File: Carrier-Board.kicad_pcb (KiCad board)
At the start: 2 copper layers, 1 part, among them X1 PC104_PLUS

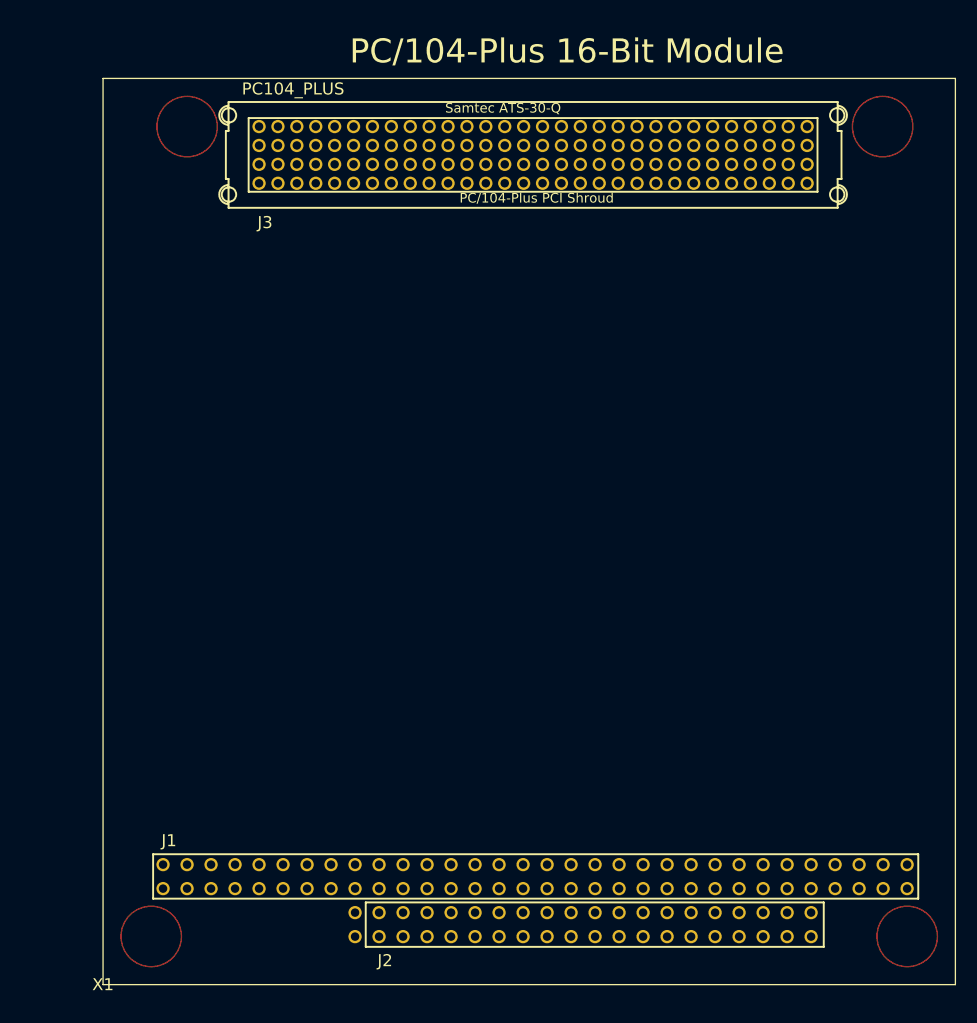
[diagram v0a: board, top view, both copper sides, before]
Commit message: Misc footprint stuff and ethernet
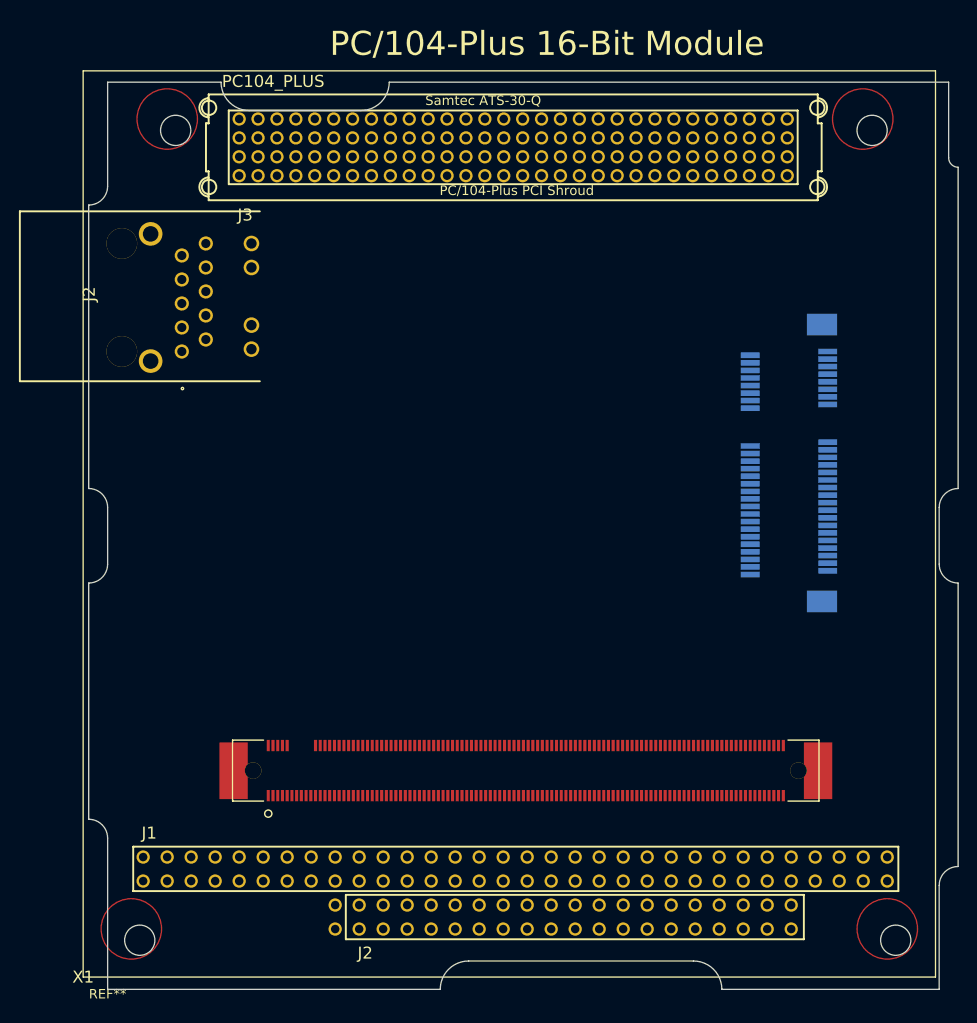
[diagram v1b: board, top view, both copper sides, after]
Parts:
- added J1: CONN_3-6318491-6, Carrier-Board:ComExpressMini10, F.Cu at (66.5, 101.7)
- added J2: SI-51009-F, Carrier-Board:SI-51009-F, F.Cu at (47.7, 54.2)
- added REF**: pc104, Carrier-Board:pc104, F.Cu at (57.0, 127.5)
- added U1: MSATA-Socket, Carrier-Board:msata-socket, B.Cu at (129.1, 59.3)
- moved X1 2.25 mm to (54.4, 126.2)
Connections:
- X1 pad A1: (no net) -> Net-(X1-PadA1)
- X1 pad A10: (no net) -> Net-(X1-PadA10)
- X1 pad A11: (no net) -> Net-(X1-PadA11)
- X1 pad A12: (no net) -> Net-(X1-PadA12)
- X1 pad A13: (no net) -> Net-(X1-PadA13)
- X1 pad A14: (no net) -> Net-(X1-PadA14)
- X1 pad A15: (no net) -> Net-(X1-PadA15)
- X1 pad A16: (no net) -> Net-(X1-PadA16)
- X1 pad A17: (no net) -> Net-(X1-PadA17)
- X1 pad A18: (no net) -> Net-(X1-PadA18)
- X1 pad A19: (no net) -> Net-(X1-PadA19)
- X1 pad A2: (no net) -> Net-(X1-PadA2)
- X1 pad A20: (no net) -> Net-(X1-PadA20)
- X1 pad A21: (no net) -> Net-(X1-PadA21)
- X1 pad A22: (no net) -> Net-(X1-PadA22)
- X1 pad A23: (no net) -> Net-(X1-PadA23)
- X1 pad A24: (no net) -> Net-(X1-PadA24)
- X1 pad A25: (no net) -> Net-(X1-PadA25)
- X1 pad A26: (no net) -> Net-(X1-PadA26)
- X1 pad A27: (no net) -> Net-(X1-PadA27)
- X1 pad A28: (no net) -> Net-(X1-PadA28)
- X1 pad A29: (no net) -> Net-(X1-PadA29)
- X1 pad A3: (no net) -> Net-(X1-PadA3)
- X1 pad A30: (no net) -> Net-(X1-PadA30)
- X1 pad A31: (no net) -> Net-(X1-PadA31)
- X1 pad A32: (no net) -> Net-(X1-PadA32)
- X1 pad A4: (no net) -> Net-(X1-PadA4)
- X1 pad A5: (no net) -> Net-(X1-PadA5)
- X1 pad A6: (no net) -> Net-(X1-PadA6)
- X1 pad A7: (no net) -> Net-(X1-PadA7)
- X1 pad A8: (no net) -> Net-(X1-PadA8)
- X1 pad A9: (no net) -> Net-(X1-PadA9)
- X1 pad B1: (no net) -> Net-(X1-PadB1)
- X1 pad B10: (no net) -> Net-(X1-PadB10)
- X1 pad B11: (no net) -> Net-(X1-PadB11)
- X1 pad B12: (no net) -> Net-(X1-PadB12)
- X1 pad B13: (no net) -> Net-(X1-PadB13)
- X1 pad B14: (no net) -> Net-(X1-PadB14)
- X1 pad B15: (no net) -> Net-(X1-PadB15)
- X1 pad B16: (no net) -> Net-(X1-PadB16)
- X1 pad B17: (no net) -> Net-(X1-PadB17)
- X1 pad B18: (no net) -> Net-(X1-PadB18)
- X1 pad B19: (no net) -> Net-(X1-PadB19)
- X1 pad B2: (no net) -> Net-(X1-PadB2)
- X1 pad B20: (no net) -> Net-(X1-PadB20)
- X1 pad B21: (no net) -> Net-(X1-PadB21)
- X1 pad B22: (no net) -> Net-(X1-PadB22)
- X1 pad B23: (no net) -> Net-(X1-PadB23)
- X1 pad B24: (no net) -> Net-(X1-PadB24)
- X1 pad B25: (no net) -> Net-(X1-PadB25)
- X1 pad B26: (no net) -> Net-(X1-PadB26)
- X1 pad B27: (no net) -> Net-(X1-PadB27)
- X1 pad B28: (no net) -> Net-(X1-PadB28)
- X1 pad B29: (no net) -> Net-(X1-PadB29)
- X1 pad B3: (no net) -> Net-(X1-PadB3)
- X1 pad B30: (no net) -> Net-(X1-PadB30)
- X1 pad B31: (no net) -> Net-(X1-PadB31)
- X1 pad B32: (no net) -> Net-(X1-PadB32)
- X1 pad B4: (no net) -> Net-(X1-PadB4)
- X1 pad B5: (no net) -> Net-(X1-PadB5)
- X1 pad B6: (no net) -> Net-(X1-PadB6)
- X1 pad B7: (no net) -> Net-(X1-PadB7)
- X1 pad B8: (no net) -> Net-(X1-PadB8)
- X1 pad B9: (no net) -> Net-(X1-PadB9)
- X1 pad C0: (no net) -> Net-(X1-PadC0)
- X1 pad C1: (no net) -> Net-(X1-PadC1)
- X1 pad C10: (no net) -> Net-(X1-PadC10)
- X1 pad C11: (no net) -> Net-(X1-PadC11)
- X1 pad C12: (no net) -> Net-(X1-PadC12)
- X1 pad C13: (no net) -> Net-(X1-PadC13)
- X1 pad C14: (no net) -> Net-(X1-PadC14)
- X1 pad C15: (no net) -> Net-(X1-PadC15)
- X1 pad C16: (no net) -> Net-(X1-PadC16)
- X1 pad C17: (no net) -> Net-(X1-PadC17)
- X1 pad C18: (no net) -> Net-(X1-PadC18)
- X1 pad C19: (no net) -> Net-(X1-PadC19)
- X1 pad C2: (no net) -> Net-(X1-PadC2)
- X1 pad C3: (no net) -> Net-(X1-PadC3)
- X1 pad C4: (no net) -> Net-(X1-PadC4)
- X1 pad C5: (no net) -> Net-(X1-PadC5)
- X1 pad C6: (no net) -> Net-(X1-PadC6)
- X1 pad C7: (no net) -> Net-(X1-PadC7)
- X1 pad C8: (no net) -> Net-(X1-PadC8)
- X1 pad C9: (no net) -> Net-(X1-PadC9)
- X1 pad D0: (no net) -> Net-(X1-PadD0)
- X1 pad D1: (no net) -> Net-(X1-PadD1)
- X1 pad D10: (no net) -> Net-(X1-PadD10)
- X1 pad D11: (no net) -> Net-(X1-PadD11)
- X1 pad D12: (no net) -> Net-(X1-PadD12)
- X1 pad D13: (no net) -> Net-(X1-PadD13)
- X1 pad D14: (no net) -> Net-(X1-PadD14)
- X1 pad D15: (no net) -> Net-(X1-PadD15)
- X1 pad D16: (no net) -> Net-(X1-PadD16)
- X1 pad D17: (no net) -> Net-(X1-PadD17)
- X1 pad D18: (no net) -> Net-(X1-PadD18)
- X1 pad D19: (no net) -> Net-(X1-PadD19)
- X1 pad D2: (no net) -> Net-(X1-PadD2)
- X1 pad D3: (no net) -> Net-(X1-PadD3)
- X1 pad D4: (no net) -> Net-(X1-PadD4)
- X1 pad D5: (no net) -> Net-(X1-PadD5)
- X1 pad D6: (no net) -> Net-(X1-PadD6)
- X1 pad D7: (no net) -> Net-(X1-PadD7)
- X1 pad D8: (no net) -> Net-(X1-PadD8)
- X1 pad D9: (no net) -> Net-(X1-PadD9)
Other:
- board outline added: 92 x 96 mm

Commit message: Remove junk from pc104
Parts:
- removed X1: PC104_PLUS, Carrier-Board:con-pc104-PC104-PLUS
- added J1: PC104_PLUS, Carrier-Board:pc104_silk, F.Cu at (54.4, 126.1)
- J2: renamed from J1; value CONN_3-6318491-6 -> PC104_PLUS
- renumbered J2 to J3
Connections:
- J2 pad 1: Net-(J1-Pad1) -> (no net)
- J2 pad 10: Net-(J1-Pad10) -> (no net)
- J2 pad 100: Net-(J1-Pad100) -> (no net)
- J2 pad 101: Net-(J1-Pad101) -> (no net)
- J2 pad 102: Net-(J1-Pad102) -> (no net)
- J2 pad 103: Net-(J1-Pad103) -> (no net)
- J2 pad 104: Net-(J1-Pad104) -> (no net)
- J2 pad 105: Net-(J1-Pad105) -> (no net)
- J2 pad 106: Net-(J1-Pad106) -> (no net)
- J2 pad 107: Net-(J1-Pad107) -> (no net)
- J2 pad 108: Net-(J1-Pad108) -> (no net)
- J2 pad 109: Net-(J1-Pad109) -> (no net)
- J2 pad 11: Net-(J1-Pad11) -> (no net)
- J2 pad 110: Net-(J1-Pad110) -> (no net)
- J2 pad 111: Net-(J1-Pad111) -> (no net)
- J2 pad 112: Net-(J1-Pad112) -> (no net)
- J2 pad 113: Net-(J1-Pad113) -> (no net)
- J2 pad 114: Net-(J1-Pad114) -> (no net)
- J2 pad 115: Net-(J1-Pad115) -> (no net)
- J2 pad 12: Net-(J1-Pad12) -> (no net)
- J2 pad 121: Net-(J1-Pad121) -> (no net)
- J2 pad 122: Net-(J1-Pad122) -> (no net)
- J2 pad 123: Net-(J1-Pad123) -> (no net)
- J2 pad 124: Net-(J1-Pad124) -> (no net)
- J2 pad 125: Net-(J1-Pad125) -> (no net)
- J2 pad 126: Net-(J1-Pad126) -> (no net)
- J2 pad 127: Net-(J1-Pad127) -> (no net)
- J2 pad 128: Net-(J1-Pad128) -> (no net)
- J2 pad 129: Net-(J1-Pad129) -> (no net)
- J2 pad 13: Net-(J1-Pad13) -> (no net)
- J2 pad 130: Net-(J1-Pad130) -> (no net)
- J2 pad 131: Net-(J1-Pad131) -> (no net)
- J2 pad 132: Net-(J1-Pad132) -> (no net)
- J2 pad 133: Net-(J1-Pad133) -> (no net)
- J2 pad 134: Net-(J1-Pad134) -> (no net)
- J2 pad 135: Net-(J1-Pad135) -> (no net)
- J2 pad 136: Net-(J1-Pad136) -> (no net)
- J2 pad 137: Net-(J1-Pad137) -> (no net)
- J2 pad 138: Net-(J1-Pad138) -> (no net)
- J2 pad 139: Net-(J1-Pad139) -> (no net)
- J2 pad 14: Net-(J1-Pad14) -> (no net)
- J2 pad 140: Net-(J1-Pad140) -> (no net)
- J2 pad 141: Net-(J1-Pad141) -> (no net)
- J2 pad 142: Net-(J1-Pad142) -> (no net)
- J2 pad 143: Net-(J1-Pad143) -> (no net)
- J2 pad 144: Net-(J1-Pad144) -> (no net)
- J2 pad 145: Net-(J1-Pad145) -> (no net)
- J2 pad 146: Net-(J1-Pad146) -> (no net)
- J2 pad 147: Net-(J1-Pad147) -> (no net)
- J2 pad 148: Net-(J1-Pad148) -> (no net)
- J2 pad 149: Net-(J1-Pad149) -> (no net)
- J2 pad 15: Net-(J1-Pad15) -> (no net)
- J2 pad 150: Net-(J1-Pad150) -> (no net)
- J2 pad 151: Net-(J1-Pad151) -> (no net)
- J2 pad 152: Net-(J1-Pad152) -> (no net)
- J2 pad 153: Net-(J1-Pad153) -> (no net)
- J2 pad 154: Net-(J1-Pad154) -> (no net)
- J2 pad 155: Net-(J1-Pad155) -> (no net)
- J2 pad 156: Net-(J1-Pad156) -> (no net)
- J2 pad 157: Net-(J1-Pad157) -> (no net)
- J2 pad 158: Net-(J1-Pad158) -> (no net)
- J2 pad 159: Net-(J1-Pad159) -> (no net)
- J2 pad 16: Net-(J1-Pad16) -> (no net)
- J2 pad 160: Net-(J1-Pad160) -> (no net)
- J2 pad 161: Net-(J1-Pad161) -> (no net)
- J2 pad 162: Net-(J1-Pad162) -> (no net)
- J2 pad 163: Net-(J1-Pad163) -> (no net)
- J2 pad 164: Net-(J1-Pad164) -> (no net)
- J2 pad 165: Net-(J1-Pad165) -> (no net)
- J2 pad 166: Net-(J1-Pad166) -> (no net)
- J2 pad 167: Net-(J1-Pad167) -> (no net)
- J2 pad 168: Net-(J1-Pad168) -> (no net)
- J2 pad 169: Net-(J1-Pad169) -> (no net)
- J2 pad 17: Net-(J1-Pad17) -> (no net)
- J2 pad 170: Net-(J1-Pad170) -> (no net)
- J2 pad 171: Net-(J1-Pad171) -> (no net)
- J2 pad 172: Net-(J1-Pad172) -> (no net)
- J2 pad 173: Net-(J1-Pad173) -> (no net)
- J2 pad 174: Net-(J1-Pad174) -> (no net)
- J2 pad 175: Net-(J1-Pad175) -> (no net)
- J2 pad 176: Net-(J1-Pad176) -> (no net)
- J2 pad 177: Net-(J1-Pad177) -> (no net)
- J2 pad 178: Net-(J1-Pad178) -> (no net)
- J2 pad 179: Net-(J1-Pad179) -> (no net)
- J2 pad 18: Net-(J1-Pad18) -> (no net)
- J2 pad 180: Net-(J1-Pad180) -> (no net)
- J2 pad 181: Net-(J1-Pad181) -> (no net)
- J2 pad 182: Net-(J1-Pad182) -> (no net)
- J2 pad 183: Net-(J1-Pad183) -> (no net)
- J2 pad 184: Net-(J1-Pad184) -> (no net)
- J2 pad 185: Net-(J1-Pad185) -> (no net)
- J2 pad 186: Net-(J1-Pad186) -> (no net)
- J2 pad 187: Net-(J1-Pad187) -> (no net)
- J2 pad 188: Net-(J1-Pad188) -> (no net)
- J2 pad 189: Net-(J1-Pad189) -> (no net)
- J2 pad 19: Net-(J1-Pad19) -> (no net)
- J2 pad 190: Net-(J1-Pad190) -> (no net)
- J2 pad 191: Net-(J1-Pad191) -> (no net)
- J2 pad 192: Net-(J1-Pad192) -> (no net)
- J2 pad 193: Net-(J1-Pad193) -> (no net)
- J2 pad 194: Net-(J1-Pad194) -> (no net)
- J2 pad 195: Net-(J1-Pad195) -> (no net)
- J2 pad 196: Net-(J1-Pad196) -> (no net)
- J2 pad 197: Net-(J1-Pad197) -> (no net)
- J2 pad 198: Net-(J1-Pad198) -> (no net)
- J2 pad 199: Net-(J1-Pad199) -> (no net)
- J2 pad 2: Net-(J1-Pad2) -> (no net)
- J2 pad 20: Net-(J1-Pad20) -> (no net)
- J2 pad 200: Net-(J1-Pad200) -> (no net)
- J2 pad 201: Net-(J1-Pad201) -> (no net)
- J2 pad 202: Net-(J1-Pad202) -> (no net)
- J2 pad 203: Net-(J1-Pad203) -> (no net)
- J2 pad 204: Net-(J1-Pad204) -> (no net)
- J2 pad 205: Net-(J1-Pad205) -> (no net)
- J2 pad 206: Net-(J1-Pad206) -> (no net)
- J2 pad 207: Net-(J1-Pad207) -> (no net)
- J2 pad 208: Net-(J1-Pad208) -> (no net)
- J2 pad 209: Net-(J1-Pad209) -> (no net)
- J2 pad 21: Net-(J1-Pad21) -> (no net)
- J2 pad 210: Net-(J1-Pad210) -> (no net)
- J2 pad 211: Net-(J1-Pad211) -> (no net)
- J2 pad 212: Net-(J1-Pad212) -> (no net)
- J2 pad 213: Net-(J1-Pad213) -> (no net)
- J2 pad 214: Net-(J1-Pad214) -> (no net)
- J2 pad 215: Net-(J1-Pad215) -> (no net)
- J2 pad 216: Net-(J1-Pad216) -> (no net)
- J2 pad 217: Net-(J1-Pad217) -> (no net)
- J2 pad 218: Net-(J1-Pad218) -> (no net)
- J2 pad 219: Net-(J1-Pad219) -> (no net)
- J2 pad 22: Net-(J1-Pad22) -> (no net)
- J2 pad 220: Net-(J1-Pad220) -> (no net)
- J2 pad 23: Net-(J1-Pad23) -> (no net)
- J2 pad 24: Net-(J1-Pad24) -> (no net)
- J2 pad 25: Net-(J1-Pad25) -> (no net)
- J2 pad 26: Net-(J1-Pad26) -> (no net)
- J2 pad 27: Net-(J1-Pad27) -> (no net)
- J2 pad 28: Net-(J1-Pad28) -> (no net)
- J2 pad 29: Net-(J1-Pad29) -> (no net)
- J2 pad 3: Net-(J1-Pad3) -> (no net)
- J2 pad 30: Net-(J1-Pad30) -> (no net)
- J2 pad 31: Net-(J1-Pad31) -> (no net)
- J2 pad 32: Net-(J1-Pad32) -> (no net)
- J2 pad 33: Net-(J1-Pad33) -> (no net)
- J2 pad 34: Net-(J1-Pad34) -> (no net)
- J2 pad 35: Net-(J1-Pad35) -> (no net)
- J2 pad 36: Net-(J1-Pad36) -> (no net)
- J2 pad 37: Net-(J1-Pad37) -> (no net)
- J2 pad 38: Net-(J1-Pad38) -> (no net)
- J2 pad 39: Net-(J1-Pad39) -> (no net)
- J2 pad 4: Net-(J1-Pad4) -> (no net)
- J2 pad 40: Net-(J1-Pad40) -> (no net)
- J2 pad 41: Net-(J1-Pad41) -> (no net)
- J2 pad 42: Net-(J1-Pad42) -> (no net)
- J2 pad 43: Net-(J1-Pad43) -> (no net)
- J2 pad 44: Net-(J1-Pad44) -> (no net)
- J2 pad 45: Net-(J1-Pad45) -> (no net)
- J2 pad 46: Net-(J1-Pad46) -> (no net)
- J2 pad 47: Net-(J1-Pad47) -> (no net)
- J2 pad 48: Net-(J1-Pad48) -> (no net)
- J2 pad 49: Net-(J1-Pad49) -> (no net)
- J2 pad 5: Net-(J1-Pad5) -> (no net)
- J2 pad 50: Net-(J1-Pad50) -> (no net)
- J2 pad 51: Net-(J1-Pad51) -> (no net)
- J2 pad 52: Net-(J1-Pad52) -> (no net)
- J2 pad 53: Net-(J1-Pad53) -> (no net)
- J2 pad 54: Net-(J1-Pad54) -> (no net)
- J2 pad 55: Net-(J1-Pad55) -> (no net)
- J2 pad 56: Net-(J1-Pad56) -> (no net)
- J2 pad 57: Net-(J1-Pad57) -> (no net)
- J2 pad 58: Net-(J1-Pad58) -> (no net)
- J2 pad 59: Net-(J1-Pad59) -> (no net)
- J2 pad 6: Net-(J1-Pad6) -> (no net)
- J2 pad 60: Net-(J1-Pad60) -> (no net)
- J2 pad 61: Net-(J1-Pad61) -> (no net)
- J2 pad 62: Net-(J1-Pad62) -> (no net)
- J2 pad 63: Net-(J1-Pad63) -> (no net)
- J2 pad 64: Net-(J1-Pad64) -> (no net)
- J2 pad 65: Net-(J1-Pad65) -> (no net)
- J2 pad 66: Net-(J1-Pad66) -> (no net)
- J2 pad 67: Net-(J1-Pad67) -> (no net)
- J2 pad 68: Net-(J1-Pad68) -> (no net)
- J2 pad 69: Net-(J1-Pad69) -> (no net)
- J2 pad 7: Net-(J1-Pad7) -> (no net)
- J2 pad 70: Net-(J1-Pad70) -> (no net)
- J2 pad 71: Net-(J1-Pad71) -> (no net)
- J2 pad 72: Net-(J1-Pad72) -> (no net)
- J2 pad 73: Net-(J1-Pad73) -> (no net)
- J2 pad 74: Net-(J1-Pad74) -> (no net)
- J2 pad 75: Net-(J1-Pad75) -> (no net)
- J2 pad 76: Net-(J1-Pad76) -> (no net)
- J2 pad 77: Net-(J1-Pad77) -> (no net)
- J2 pad 78: Net-(J1-Pad78) -> (no net)
- J2 pad 79: Net-(J1-Pad79) -> (no net)
- J2 pad 8: Net-(J1-Pad8) -> (no net)
- J2 pad 80: Net-(J1-Pad80) -> (no net)
- J2 pad 81: Net-(J1-Pad81) -> (no net)
- J2 pad 82: Net-(J1-Pad82) -> (no net)
- J2 pad 83: Net-(J1-Pad83) -> (no net)
- J2 pad 84: Net-(J1-Pad84) -> (no net)
- J2 pad 85: Net-(J1-Pad85) -> (no net)
- J2 pad 86: Net-(J1-Pad86) -> (no net)
- J2 pad 87: Net-(J1-Pad87) -> (no net)
- J2 pad 88: Net-(J1-Pad88) -> (no net)
- J2 pad 89: Net-(J1-Pad89) -> (no net)
- J2 pad 9: Net-(J1-Pad9) -> (no net)
- J2 pad 90: Net-(J1-Pad90) -> (no net)
- J2 pad 91: Net-(J1-Pad91) -> (no net)
- J2 pad 92: Net-(J1-Pad92) -> (no net)
- J2 pad 93: Net-(J1-Pad93) -> (no net)
- J2 pad 94: Net-(J1-Pad94) -> (no net)
- J2 pad 95: Net-(J1-Pad95) -> (no net)
- J2 pad 96: Net-(J1-Pad96) -> (no net)
- J2 pad 97: Net-(J1-Pad97) -> (no net)
- J2 pad 98: Net-(J1-Pad98) -> (no net)
- J2 pad 99: Net-(J1-Pad99) -> (no net)
- J3 pad 1: Net-(J2-Pad1) -> (no net)
- J3 pad 10: Net-(J2-Pad10) -> (no net)
- J3 pad 2: Net-(J2-Pad2) -> (no net)
- J3 pad 3: Net-(J2-Pad3) -> (no net)
- J3 pad 4: Net-(J2-Pad4) -> (no net)
- J3 pad 5: Net-(J2-Pad5) -> (no net)
- J3 pad 6: Net-(J2-Pad6) -> (no net)
- J3 pad 7: Net-(J2-Pad7) -> (no net)
- J3 pad 8: Net-(J2-Pad8) -> (no net)
- J3 pad 9: Net-(J2-Pad9) -> (no net)
- U1 pad 1: Net-(U1-Pad1) -> (no net)
- U1 pad 10: Net-(U1-Pad10) -> (no net)
- U1 pad 11: Net-(U1-Pad11) -> (no net)
- U1 pad 12: Net-(U1-Pad12) -> (no net)
- U1 pad 13: Net-(U1-Pad13) -> (no net)
- U1 pad 14: Net-(U1-Pad14) -> (no net)
- U1 pad 15: Net-(U1-Pad15) -> (no net)
- U1 pad 16: Net-(U1-Pad16) -> (no net)
- U1 pad 17: Net-(U1-Pad17) -> (no net)
- U1 pad 18: Net-(U1-Pad18) -> (no net)
- U1 pad 19: Net-(U1-Pad19) -> (no net)
- U1 pad 2: Net-(U1-Pad2) -> (no net)
- U1 pad 20: Net-(U1-Pad20) -> (no net)
- U1 pad 21: Net-(U1-Pad21) -> (no net)
- U1 pad 22: Net-(U1-Pad22) -> (no net)
- U1 pad 23: Net-(U1-Pad23) -> (no net)
- U1 pad 24: Net-(U1-Pad24) -> (no net)
- U1 pad 25: Net-(U1-Pad25) -> (no net)
- U1 pad 26: Net-(U1-Pad26) -> (no net)
- U1 pad 27: Net-(U1-Pad27) -> (no net)
- U1 pad 28: Net-(U1-Pad28) -> (no net)
- U1 pad 29: Net-(U1-Pad29) -> (no net)
- U1 pad 3: Net-(U1-Pad3) -> (no net)
- U1 pad 30: Net-(U1-Pad30) -> (no net)
- U1 pad 31: Net-(U1-Pad31) -> (no net)
- U1 pad 32: Net-(U1-Pad32) -> (no net)
- U1 pad 33: Net-(U1-Pad33) -> (no net)
- U1 pad 34: Net-(U1-Pad34) -> (no net)
- U1 pad 35: Net-(U1-Pad35) -> (no net)
- U1 pad 36: Net-(U1-Pad36) -> (no net)
- U1 pad 37: Net-(U1-Pad37) -> (no net)
- U1 pad 38: Net-(U1-Pad38) -> (no net)
- U1 pad 39: Net-(U1-Pad39) -> (no net)
- U1 pad 4: Net-(U1-Pad4) -> (no net)
- U1 pad 40: Net-(U1-Pad40) -> (no net)
- U1 pad 41: Net-(U1-Pad41) -> (no net)
- U1 pad 42: Net-(U1-Pad42) -> (no net)
- U1 pad 43: Net-(U1-Pad43) -> (no net)
- U1 pad 44: Net-(U1-Pad44) -> (no net)
- U1 pad 45: Net-(U1-Pad45) -> (no net)
- U1 pad 46: Net-(U1-Pad46) -> (no net)
- U1 pad 47: Net-(U1-Pad47) -> (no net)
- U1 pad 48: Net-(U1-Pad48) -> (no net)
- U1 pad 49: Net-(U1-Pad49) -> (no net)
- U1 pad 5: Net-(U1-Pad5) -> (no net)
- U1 pad 50: Net-(U1-Pad50) -> (no net)
- U1 pad 51: Net-(U1-Pad51) -> (no net)
- U1 pad 52: Net-(U1-Pad52) -> (no net)
- U1 pad 6: Net-(U1-Pad6) -> (no net)
- U1 pad 7: Net-(U1-Pad7) -> (no net)
- U1 pad 8: Net-(U1-Pad8) -> (no net)
- U1 pad 9: Net-(U1-Pad9) -> (no net)

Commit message: 'kidz
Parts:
- moved U1 0.06 mm to (129.1, 59.4)
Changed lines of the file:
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@@
     (links 116)
     (no_connects 116)
-    (area 0 0 0 0)
+    (area 41.471239 29.878679 157.492041 139.003381)
     (thickness 1.6)
     (drawings 0)
@@
   )
   (module Carrier-Board:msata-socket (layer B.Cu)
-    (at 129.1 59.3 270)
+    (at 129.075 59.35 270)
     (tags "mpci, pci, pci express")
     (fp_text reference U1 (at 30.45 -2.45 540) (layer B.SilkS) hide

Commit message: added footprints
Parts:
- removed J2: PC104_PLUS, Carrier-Board:ComExpressMini10
- added C1: 10uF, BusSimulator:C22, F.Cu at (308.4, 86.2)
- added C2: 22uF, BusSimulator:C22, F.Cu at (316.7, 84.8)
- added C27: .1uF, Capacitors_SMD:C_0603, F.Cu at (262.3, 141.3)
- added C28: .1uF, Capacitors_SMD:C_0603, F.Cu at (322.7, 84.1)
- added C29: .1uF, Capacitors_SMD:C_0603, F.Cu at (252.7, 152.4)
- added C3: 10uF, BusSimulator:C22, F.Cu at (308.4, 79.9)
- added C4: 22uF, BusSimulator:C22, F.Cu at (264.7, 135.6)
- added D5: D_Zener 9V, Diodes_SMD:D_SOD-323, F.Cu at (308.4, 74.2)
- added D6: LED, Diodes_SMD:D_1206, F.Cu at (292.5, 110.3)
- added D7: LED, Diodes_SMD:D_1206, F.Cu at (253.4, 146.9)
- added D8: LED, Diodes_SMD:D_1206, F.Cu at (306.7, 92.1)
- added G1: LOGO, BusSimulator:LetSatLogo440, F.Cu at (261.7, 110.5)
- added J4: SI-51009-F, Carrier-Board:SI-51009-F, F.Cu at (247.3, 122.3)
- added J5: Conn_02x26_Odd_Even, Carrier-Board:ESQ-126-XX-X-D, F.Cu at (128.0, 35.5)
- added J6: Conn_01x03_Male, Pin_Headers:Pin_Header_Angled_1x03_Pitch2.54mm, F.Cu at (278.8, 110.8)
- added J7: Conn_01x03_Male, Pin_Headers:Pin_Header_Angled_1x03_Pitch2.54mm, F.Cu at (249.3, 135.7)
- added J8: Conn_01x06_Male, Pin_Headers:Pin_Header_Angled_1x06_Pitch2.54mm, F.Cu at (317.1, 65.6)
- added R1: 160k, Resistors_SMD:R_0805, F.Cu at (279.1, 121.8)
- added R10: 10k, Resistors_SMD:R_0603, F.Cu at (265.8, 141.2)
- added R11: 30k, Resistors_SMD:R_0603, F.Cu at (291.6, 115.7)
- added R12: 10k, Resistors_SMD:R_0603, F.Cu at (270.5, 134.9)
- added R2: 30.1k, Resistors_SMD:R_0805, F.Cu at (314.8, 90.5)
- added R23: 330, Resistors_SMD:R_0603, F.Cu at (330.0, 75.7)
- added R24: 180, Resistors_SMD:R_0603, F.Cu at (278.2, 128.2)
- added R25: 1k, Resistors_SMD:R_0603, F.Cu at (248.5, 158.5)
- added R3: 100k, Resistors_SMD:R_0805, F.Cu at (283.1, 121.8)
- added R32: 0, Resistors_SMD:R_0805, F.Cu at (330.1, 70.4)
- added R4: 63.4k, Resistors_SMD:R_0805, F.Cu at (306.5, 97.7)
- added R5: 160k, Resistors_SMD:R_0805, F.Cu at (258.0, 146.8)
- added R6: 51k, Resistors_SMD:R_0805, F.Cu at (330.1, 65.0)
- added R7: 100k, Resistors_SMD:R_0805, F.Cu at (248.9, 153.3)
- added R8: 56k, Resistors_SMD:R_0805, F.Cu at (274.8, 128.4)
- added R9: 10k, Resistors_SMD:R_0603, F.Cu at (274.6, 115.5)
- added U2: MPM3620, BusSimulator:QFN-20, F.Cu at (248.9, 147.2)
- added U9: MSATA-Socket, BusSimulator:msata-socket, B.Cu at (253.1, 103.1)
- J1: value PC104_PLUS -> CONN_3-6318491-6; footprint Carrier-Board:pc104_silk -> BusSimulator:ComExpressMini10
- J3: value SI-51009-F -> Conn_02x26_Odd_Even; footprint Carrier-Board:SI-51009-F -> Carrier-Board:ESQ-126-XX-X-D
- U1: value MSATA-Socket -> MPM3620; footprint Carrier-Board:msata-socket -> BusSimulator:QFN-20; moved to F.Cu
- moved J1 265.8 mm to (314.2, 70.2), turned to 180 degrees
- moved U1 158.9 mm to (275.0, 122.2), turned to 0 degrees
- moved REF** 104.4 mm to (156.6, 158.6)
- moved J3 83.7 mm to (128.0, 30.4), turned to 0 degrees
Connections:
- J3 pad 1: (no net) -> Net-(J3-Pad1)
- J3 pad 10: (no net) -> Net-(J3-Pad10)
- J3 pad 11: (no net) -> Net-(J3-Pad11)
- J3 pad 12: (no net) -> Net-(J3-Pad12)
- J3 pad 13: (no net) -> Net-(J3-Pad13)
- J3 pad 14: (no net) -> Net-(J3-Pad14)
- J3 pad 15: (no net) -> Net-(J3-Pad15)
- J3 pad 16: (no net) -> Net-(J3-Pad16)
- J3 pad 17: (no net) -> Net-(J3-Pad17)
- J3 pad 18: (no net) -> Net-(J3-Pad18)
- J3 pad 2: (no net) -> Net-(J3-Pad2)
- J3 pad 3: (no net) -> Net-(J3-Pad3)
- J3 pad 4: (no net) -> Net-(J3-Pad4)
- J3 pad 5: (no net) -> Net-(J3-Pad5)
- J3 pad 6: (no net) -> Net-(J3-Pad6)
- J3 pad 7: (no net) -> Net-(J3-Pad7)
- J3 pad 8: (no net) -> Net-(J3-Pad8)
- J3 pad 9: (no net) -> Net-(J3-Pad9)
- U1 pad 1: (no net) -> Net-(R1-Pad2)
- U1 pad 11: (no net) -> Net-(U1-Pad11)
- U1 pad 12: (no net) -> mCOM_GND
- U1 pad 13: (no net) -> mCOM_GND
- U1 pad 14: (no net) -> mCOM_GND
- U1 pad 16: (no net) -> 12v_sense
- U1 pad 17: (no net) -> Net-(R3-Pad2)
- U1 pad 18: (no net) -> Net-(R4-Pad1)
- U1 pad 2: (no net) -> Net-(U1-Pad2)
- U1 pad 3: (no net) -> GNDA
- U1 pad 4: (no net) -> Net-(U1-Pad4)
- U1 pad 5: (no net) -> Net-(U1-Pad5)
- U1 pad 6: (no net) -> Net-(U1-Pad6)
- U1 pad 7: (no net) -> mCOM_5V_SBY
- U1 pad 8: (no net) -> mCOM_5V_SBY
- U1 pad 9: (no net) -> mCOM_5V_SBY
